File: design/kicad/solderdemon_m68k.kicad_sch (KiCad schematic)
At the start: 0 parts

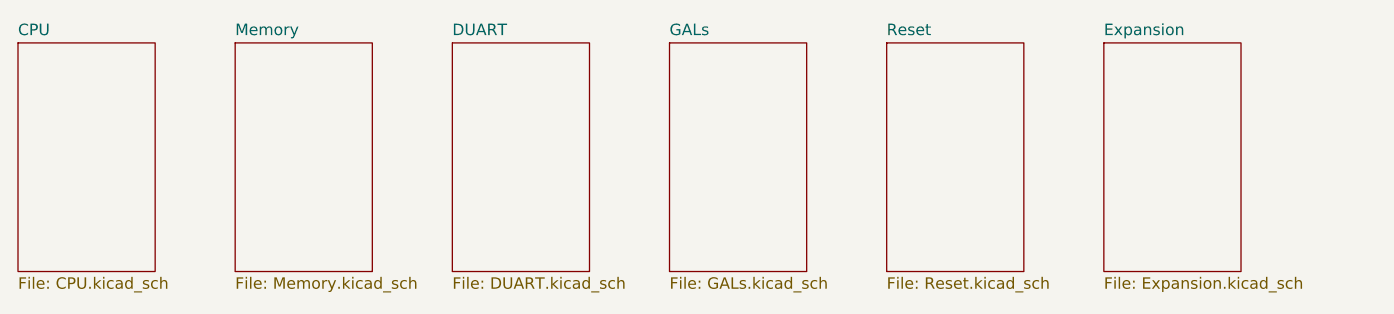
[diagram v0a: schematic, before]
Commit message: SolderDemon m68k r2.42: CPLD board, rebranding and silkscreen cleanup
Rename the KiCad project to solderdemon_m68k and move the glue logic
to two ATF1502AS CPLDs, with generator/routing scripts in design/tools.

Remove the upstream silkscreen badges (WEEE bin, OSHW certification
block, rosco_m68k logos, GitHub URL next to the expansion connector)
and bump the copyright to 2019-2026 via design/tools/strip_silk.py.
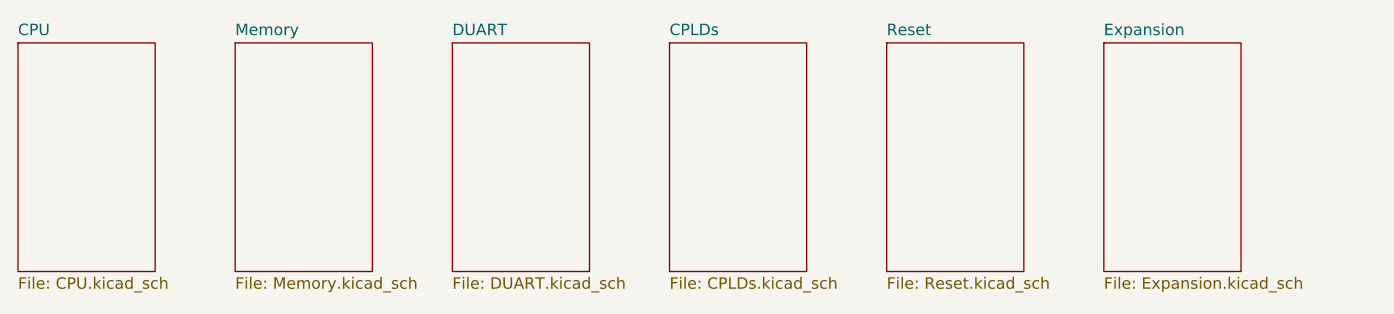
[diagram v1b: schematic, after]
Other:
- sheet GALs renamed CPLDs
- sheet CPLDs: file GALs.kicad_sch -> CPLDs.kicad_sch
- company: The Really Old-School Company Limited -> SolderDemon
- title: ROSCO_M68K GENERAL PURPOSE MC68010 COMPUTER -> SolderDemon m68k Classic v2
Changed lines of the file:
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@@
   (paper "A4")
   (title_block
-    (title "ROSCO_M68K GENERAL PURPOSE MC68010 COMPUTER")
-    (date "2023-12-10")
-    (rev "2.13-DEV")
-    (company "The Really Old-School Company Limited")
+    (title "SolderDemon m68k Classic v2")
+    (date "2026-09-28")
+    (rev "2.42")
+    (company "SolderDemon")
     (comment 1 "OSHWA UK000006 (https://certification.oshwa.org/uk000006.html)")
     (comment 2 "See https://github.com/roscopeco/rosco_m68k/blob/master/LICENCE.hardware.txt")
     (comment 3 "Open Source Hardware licenced under CERN Open Hardware Licence")
     (comment 4 "Copyright 2019-2023 Ross Bamford and Contributors")
+    (comment 5 "SolderDemon modification 2026-09-28; based on rosco_m68k")
   )
   (sheet (at 81.28 81.28) (size 15.24 25.4) (fields_autoplaced)
@@
     )
     (instances
-      (project "rosco_m68k"
+      (project "solderdemon_m68k"
         (path "/9031bb33-c6aa-4758-bf5c-3274ed3ebab7" (page "2"))
       )
@@
     )
     (instances
-      (project "rosco_m68k"
+      (project "solderdemon_m68k"
         (path "/9031bb33-c6aa-4758-bf5c-3274ed3ebab7" (page "4"))
       )
@@
     )
     (instances
-      (project "rosco_m68k"
+      (project "solderdemon_m68k"
         (path "/9031bb33-c6aa-4758-bf5c-3274ed3ebab7" (page "3"))
       )
@@
     )
     (instances
-      (project "rosco_m68k"
+      (project "solderdemon_m68k"
         (path "/9031bb33-c6aa-4758-bf5c-3274ed3ebab7" (page "7"))
       )
@@
     )
     (instances
-      (project "rosco_m68k"
+      (project "solderdemon_m68k"
         (path "/9031bb33-c6aa-4758-bf5c-3274ed3ebab7" (page "6"))
       )
@@
     (stroke (width 0) (type solid))
     (fill (color 0 0 0 0.0000))
-    (property "Sheetname" "GALs" (at 153.67 80.5684 0)
+    (property "Sheetname" "CPLDs" (at 153.67 80.5684 0)
       (effects (font (size 1.27 1.27)) (justify left bottom))
     )
-    (property "Sheetfile" "GALs.kicad_sch" (at 153.67 107.2646 0)
+    (property "Sheetfile" "CPLDs.kicad_sch" (at 153.67 107.2646 0)
       (effects (font (size 1.27 1.27)) (justify left top))
     )
     (instances
-      (project "rosco_m68k"
+      (project "solderdemon_m68k"
         (path "/9031bb33-c6aa-4758-bf5c-3274ed3ebab7" (page "5"))
       )
